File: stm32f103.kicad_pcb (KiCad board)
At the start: 2 copper layers, 134.5 x 97 mm, 87 parts, among them J1 12Vin, J11 Button, J12 Load, J2 SYSTEM_BOOT_JUMP, J3 ADC_PIN, J4 BOOTLOADER_UART, J5 MY_BOOT_JUMP, J6 ARM_JTAG, J7 USB_B_MINI, J8 Magnet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

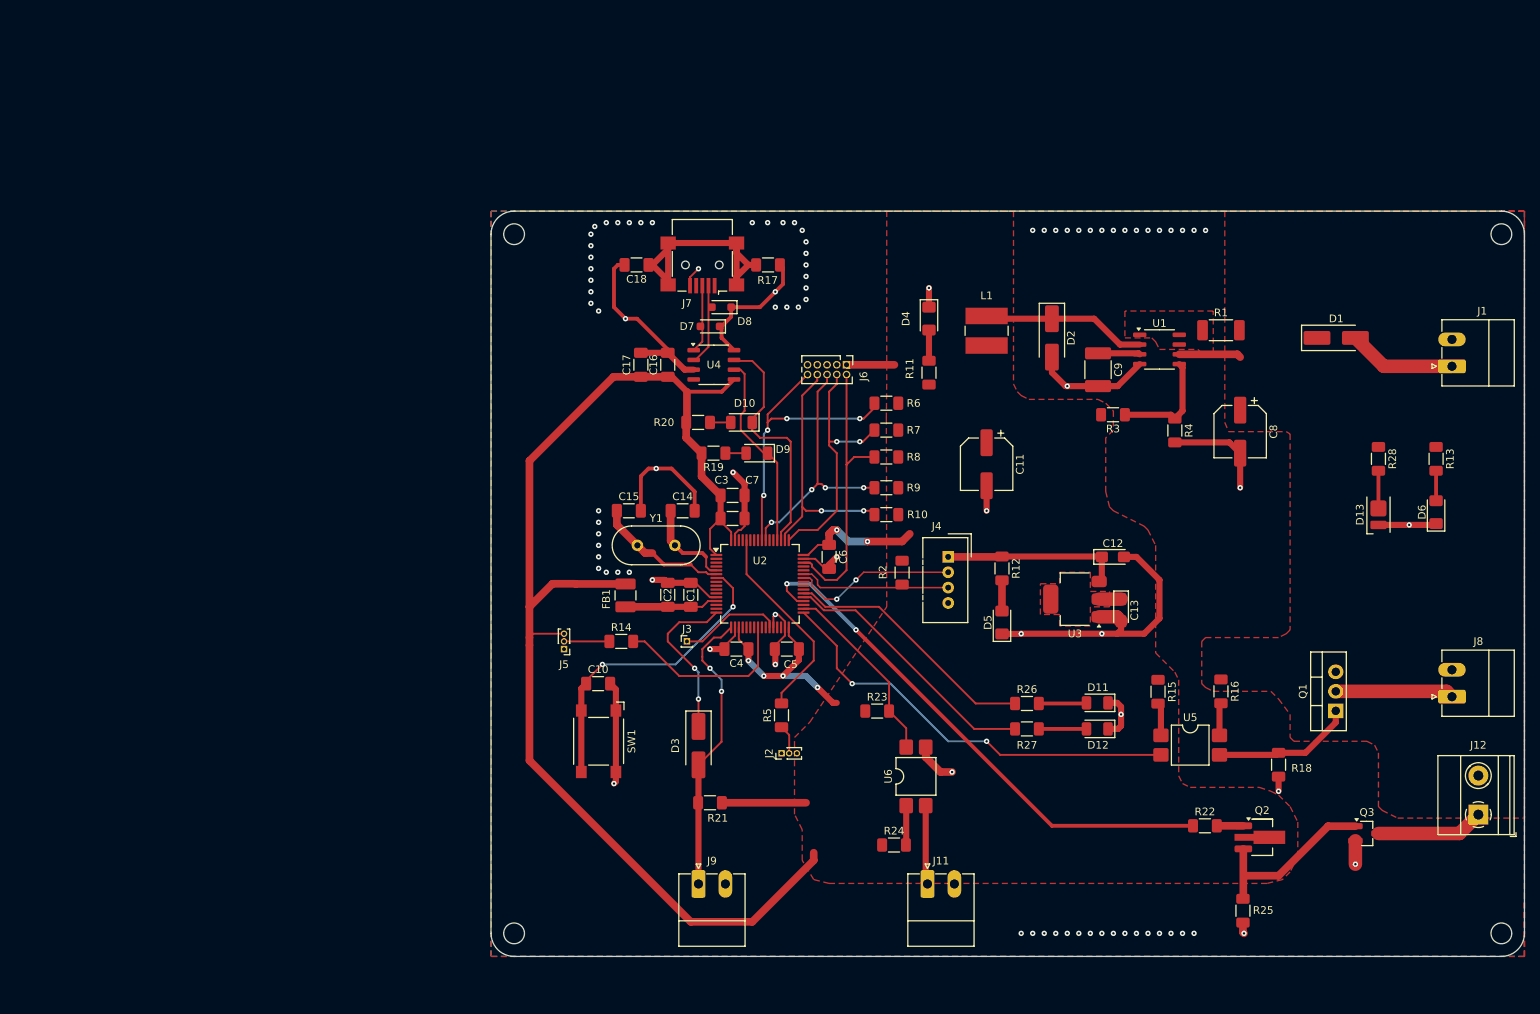
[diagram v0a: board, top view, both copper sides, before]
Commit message: Stack has been chosen: 4 layer SIG+GND+PWR+SIG. Componetns have been divided in groups pcb
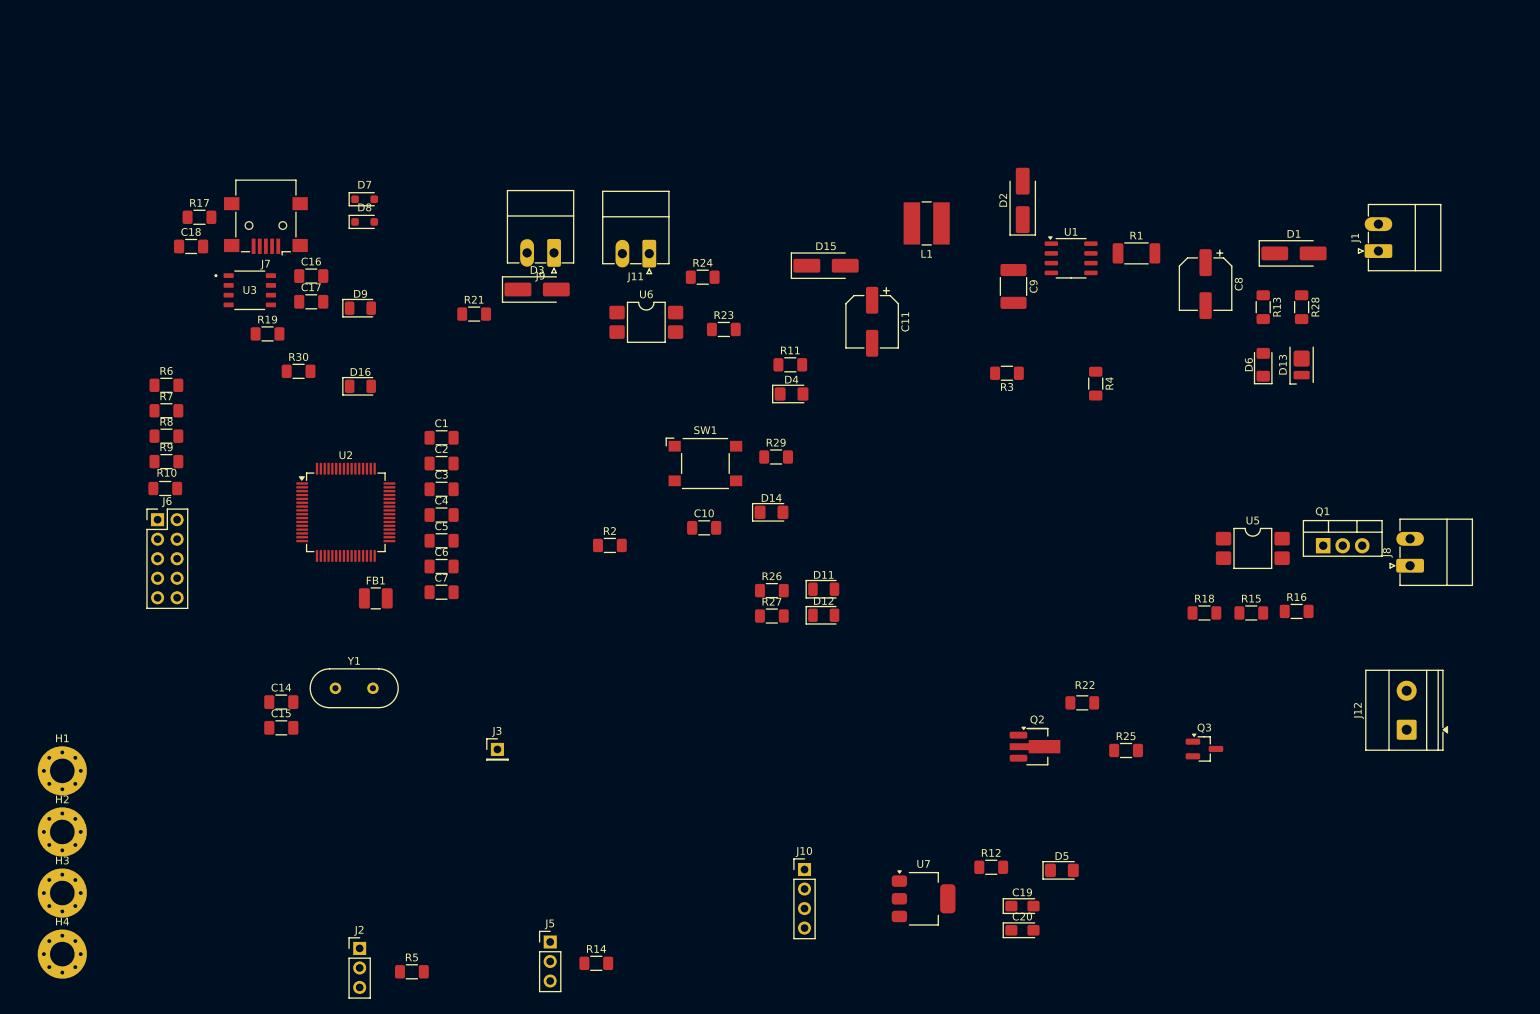
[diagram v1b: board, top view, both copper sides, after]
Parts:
- removed C12: 10u, Capacitor_Tantalum_SMD:CP_EIA-3216-12_Kemet-S_HandSolder
- removed C13: 22u, Capacitor_Tantalum_SMD:CP_EIA-3216-12_Kemet-S_HandSolder
- removed D10: LED_yellow, LED_SMD:LED_1206_3216Metric
- removed J4: BOOTLOADER_UART, Connector:NS-Tech_Grove_1x04_P2mm_Vertical
- removed R20: 1k, Resistor_SMD:R_1206_3216Metric_Pad1.30x1.75mm_HandSolder
- removed U4: CH340N, Package_SO:SOP-8_3.9x4.9mm_P1.27mm
- added C19: 10u, Capacitor_Tantalum_SMD:CP_EIA-3216-12_Kemet-S_HandSolder, F.Cu at (169.2, 131.9)
- added C20: 22u, Capacitor_Tantalum_SMD:CP_EIA-3216-12_Kemet-S_HandSolder, F.Cu at (169.2, 135.1)
- added D14: LED_red, LED_SMD:LED_1206_3216Metric_Pad1.42x1.75mm_HandSolder, F.Cu at (136.5, 80.7)
- added D15: B340LA-13-F, Diode_SMD:D_SMA_Handsoldering, F.Cu at (143.6, 48.6)
- added D16: LED_yellow, LED_SMD:LED_1206_3216Metric, F.Cu at (83.0, 64.3)
- added J10: BOOTLOADER_UART, Connector_PinHeader_2.54mm:PinHeader_1x04_P2.54mm_Vertical, F.Cu at (140.8, 127.2)
- added R29: 400, Resistor_SMD:R_1206_3216Metric_Pad1.30x1.75mm_HandSolder, F.Cu at (137.1, 73.5)
- added R30: 1k, Resistor_SMD:R_1206_3216Metric_Pad1.30x1.75mm_HandSolder, F.Cu at (75.0, 62.4)
- added U7: AMS1117-3.3, Package_TO_SOT_SMD:SOT-223-3_TabPin2, F.Cu at (156.3, 131.0)
- H1, H2, H3, H4: value MountingHole -> MountingHole_Pad; footprint MountingHole:MountingHole_2.7mm_M2.5_ISO14580 -> MountingHole:MountingHole_3.2mm_M3_Pad_Via
- J2, J5: footprint Connector_PinHeader_1.00mm:PinHeader_1x03_P1.00mm_Vertical -> Connector_PinHeader_2.54mm:PinHeader_1x03_P2.54mm_Vertical
- J3: footprint Connector_PinHeader_1.00mm:PinHeader_1x01_P1.00mm_Vertical -> Connector_PinHeader_2.54mm:PinHeader_1x01_P2.54mm_Vertical
- J6: footprint Connector_PinHeader_1.27mm:PinHeader_2x05_P1.27mm_Vertical -> Connector_PinHeader_2.54mm:PinHeader_2x05_P2.54mm_Vertical
- L1: value 3.85u CDSP43-4R7M -> 50u CDSP43-4R7M
- R3: value 4.920k -> 6.2k
- U3: value AMS1117-3.3 -> CH340N; footprint Package_TO_SOT_SMD:SOT-223-3_TabPin2 -> CH340N:SOIC127P600X160-8N
- moved H2 202.8 mm to (44.2, 122.3)
- moved H1 188.5 mm to (44.2, 114.3)
- moved U3 114.7 mm to (68.6, 51.8), turned to 0 degrees
- moved H3 104.0 mm to (44.2, 130.2)
- moved R10 93.9 mm to (57.6, 77.6), turned to 0 degrees
- moved R9 93.8 mm to (57.8, 74.1), turned to 0 degrees
- moved R8 93.7 mm to (57.8, 70.8), turned to 0 degrees
- moved R7 93.7 mm to (57.8, 67.5), turned to 0 degrees
- moved R6 93.7 mm to (57.8, 64.2), turned to 0 degrees
- moved J6 91.9 mm to (56.6, 81.7), turned to 0 degrees
- moved J11 89.7 mm to (120.6, 47.0), turned to 180 degrees
- moved J9 84.3 mm to (108.2, 46.9), turned to 180 degrees
- moved R24 78.0 mm to (127.5, 50.1)
- moved R17 74.3 mm to (62.0, 42.3), turned to 0 degrees
- moved R21 70.6 mm to (97.8, 54.9), turned to 0 degrees
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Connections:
- C11 pad 1: +3.3V -> Net-(D15-A)
- L1 pad 2: +3.3V -> Net-(D15-A)
- R3 pad 2: +3.3V -> Net-(D15-A)
- U3 pad 1: GND -> Net-(D7-A2)
- U3 pad 2: +3.3V -> Net-(D8-A2)
- U3 pad 3: +5V -> GND
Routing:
- net +3.3V: track 231.9 -> 0.00 mm, vias 6 -> 0
- net GND: track 212.4 -> 0.00 mm, vias 92 -> 0
- net PWM_MOSFET: track 69.6 -> 0.00 mm, vias 2 -> 0
- net PB12: track 55.9 -> 0.00 mm, vias 2 -> 0
- net Net-(D14-K): track 40.4 -> 0.00 mm, vias 2 -> 0
- net RESET: track 39.4 -> 0.00 mm, vias 4 -> 0
- net USART2_TX_RX: track 37.8 -> 0.00 mm, vias 2 -> 0
- net TMS: track 36.7 -> 0.00 mm
- net Net-(J7-Shield): track 35.2 -> 0.00 mm
- net LED_PB11: track 34.6 -> 0.00 mm
- net LED_PB10: track 33.5 -> 0.00 mm
- net TDO: track 33.1 -> 0.00 mm, vias 4 -> 0
- net TCLK: track 32.9 -> 0.00 mm, vias 2 -> 0
- net TDI: track 32.9 -> 0.00 mm, vias 2 -> 0
- net USART3_TX: track 31.6 -> 0.00 mm
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- removed copper zone on F.Cu, net +12V
- removed copper zone on F.Cu, net +3.3V
- removed copper zone on B.Cu, net GND
- removed copper zone on F.Cu, net GND
- removed copper zone on F.Cu, net Net-(U1-DC)
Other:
- board outline removed
- copper layers 2 -> 4

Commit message: Shottky diod has been added to provide protection for AMS1117-3.3
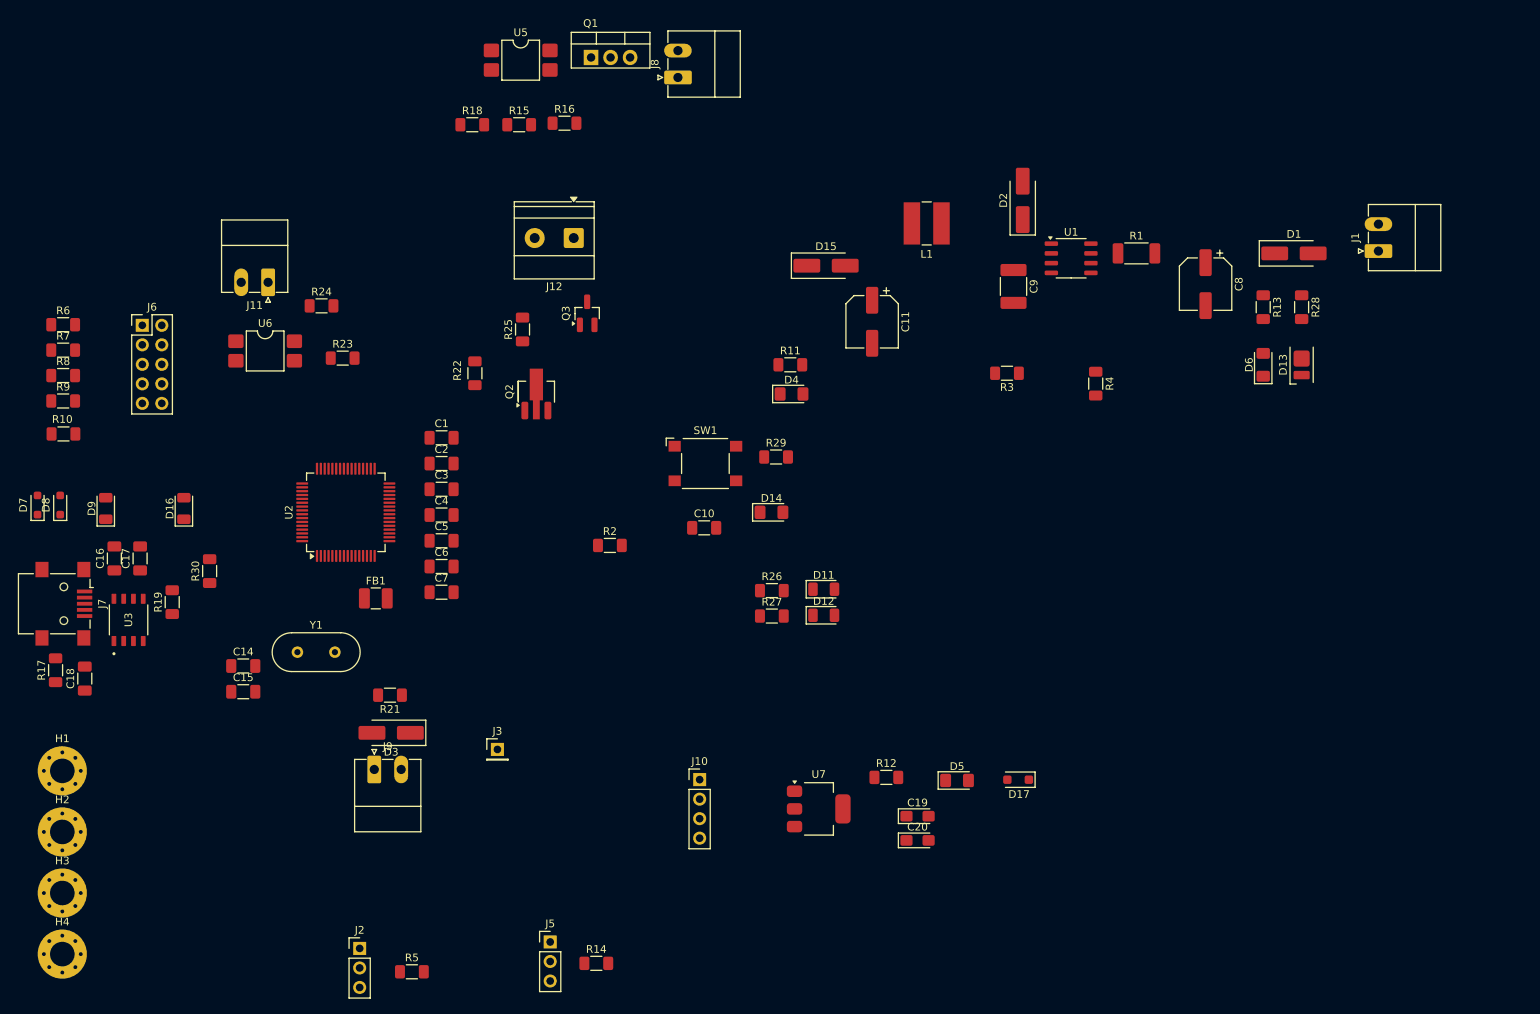
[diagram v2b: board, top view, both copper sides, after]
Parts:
- added D17: SM5819PL-TP, Diode_SMD:D_SOD-123F, F.Cu at (168.6, 115.5)
- C9: value 40n -> 1n
- moved J12 125.9 mm to (110.8, 45.0), turned to 180 degrees
- moved J8 114.5 mm to (124.3, 24.1)
- moved Q1 114.5 mm to (113.0, 21.5)
- moved R15 114.5 mm to (103.7, 30.3)
- moved R18 114.5 mm to (97.6, 30.3)
- moved U5 114.5 mm to (103.9, 21.9)
- moved R16 114.5 mm to (109.6, 30.1)
- moved Q3 98.3 mm to (112.5, 54.8), turned to 90 degrees
- moved R25 95.8 mm to (104.1, 56.9), turned to 90 degrees
- moved R22 89.9 mm to (97.9, 62.6), turned to 90 degrees
- moved Q2 79.9 mm to (105.9, 65.0), turned to 90 degrees
- moved J9 71.2 mm to (84.8, 114.2), turned to 0 degrees
- moved R17 61.9 mm to (43.3, 101.2), turned to 90 degrees
- moved D3 60.7 mm to (87.0, 109.4), turned to 180 degrees
- moved D7 58.3 mm to (41.0, 79.8), turned to 90 degrees
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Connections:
- C20 pad 1: +3.3V -> Net-(D17-A)
- J12 pad 1: Net-(J12-Pin_2) -> +12V
- J12 pad 2: +12V -> Net-(J12-Pin_2)
- U7 pad 2: +3.3V -> Net-(D17-A)
